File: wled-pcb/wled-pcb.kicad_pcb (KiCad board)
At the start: 2 copper layers, 90.2 x 90.2 mm, 36 parts, among them J2 Conn_02x03_Counter_Clockwise, J3 Screw_Terminal_01x03, J4 Screw_Terminal_01x03, J5 Screw_Terminal_01x03, J6 Screw_Terminal_01x02, J7 Screw_Terminal_01x03, K1 Relay_SPDT, Q1 BC337, SW1 SW_Push, SW2 SW_Push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

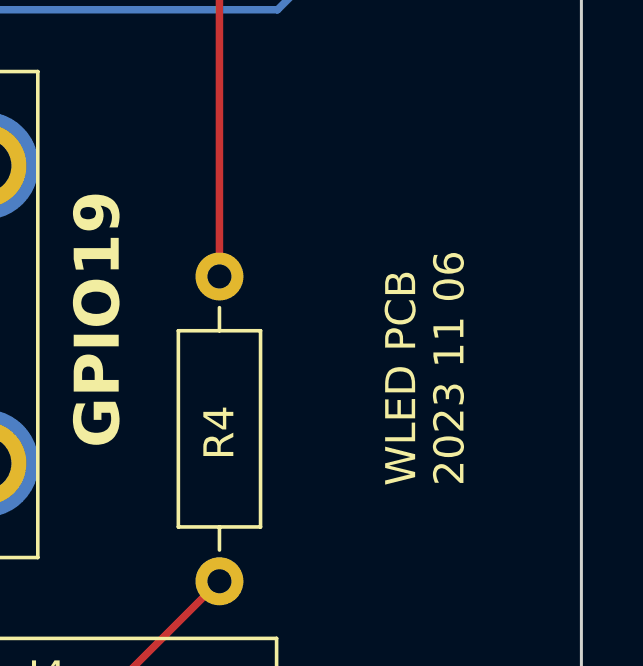
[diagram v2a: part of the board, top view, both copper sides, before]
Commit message: Rotate spokes to pass DRC
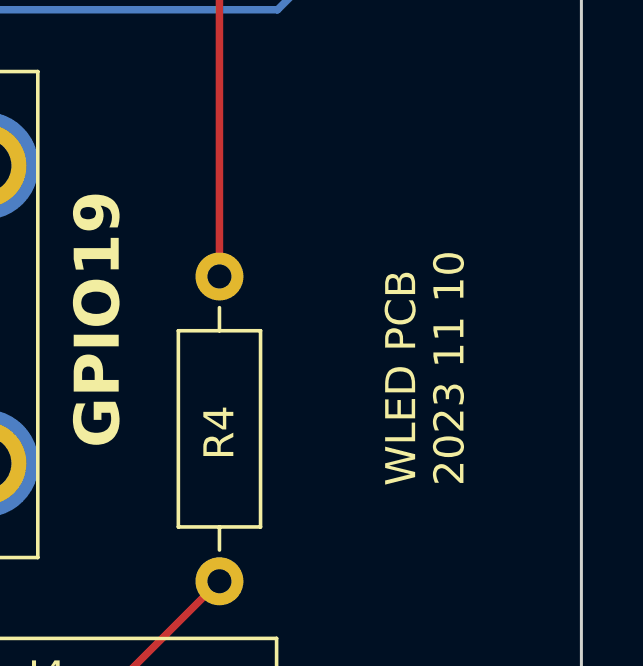
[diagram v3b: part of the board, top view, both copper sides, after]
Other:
- board text added: "WLED PCB 2023 11 10"
- board text removed: "WLED PCB 2023 11 06"
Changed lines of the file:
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@@
       (net 56 "/led3 lo") (pinfunction "D") (pintype "input"))
     (pad "10" thru_hole oval (at 7.62 10.16 90) (size 2.4 1.6) (drill 0.8) (layers "*.Cu" "*.Mask")
-      (net 2 "GND") (pinfunction "EN") (pintype "input"))
+      (net 2 "GND") (pinfunction "EN") (pintype "input") (thermal_bridge_angle 45))
     (pad "11" thru_hole oval (at 7.62 7.62 90) (size 2.4 1.6) (drill 0.8) (layers "*.Cu" "*.Mask")
       (net 26 "Net-(U2D-O)") (pinfunction "O") (pintype "tri_state"))
@@
       (net 39 "/led4 lo") (pinfunction "D") (pintype "input"))
     (pad "13" thru_hole oval (at 7.62 2.54 90) (size 2.4 1.6) (drill 0.8) (layers "*.Cu" "*.Mask")
-      (net 2 "GND") (pinfunction "EN") (pintype "input"))
+      (net 2 "GND") (pinfunction "EN") (pintype "input") (thermal_bridge_angle 45))
     (pad "14" thru_hole oval (at 7.62 0 90) (size 2.4 1.6) (drill 0.8) (layers "*.Cu" "*.Mask")
       (net 1 "+5V") (pinfunction "VCC") (pintype "power_in"))
@@
     (effects (font (size 1.5 1.5) (thickness 0.3) bold) (justify left bottom))
   )
-  (gr_text "WLED PCB\n2023 11 06" (at 180.975 128.27 90) (layer "F.SilkS")
+  (gr_text "WLED PCB\n2023 11 10" (at 180.975 128.27 90) (layer "F.SilkS")
     (effects (font (size 1 1) (thickness 0.15)) (justify left bottom))
   )

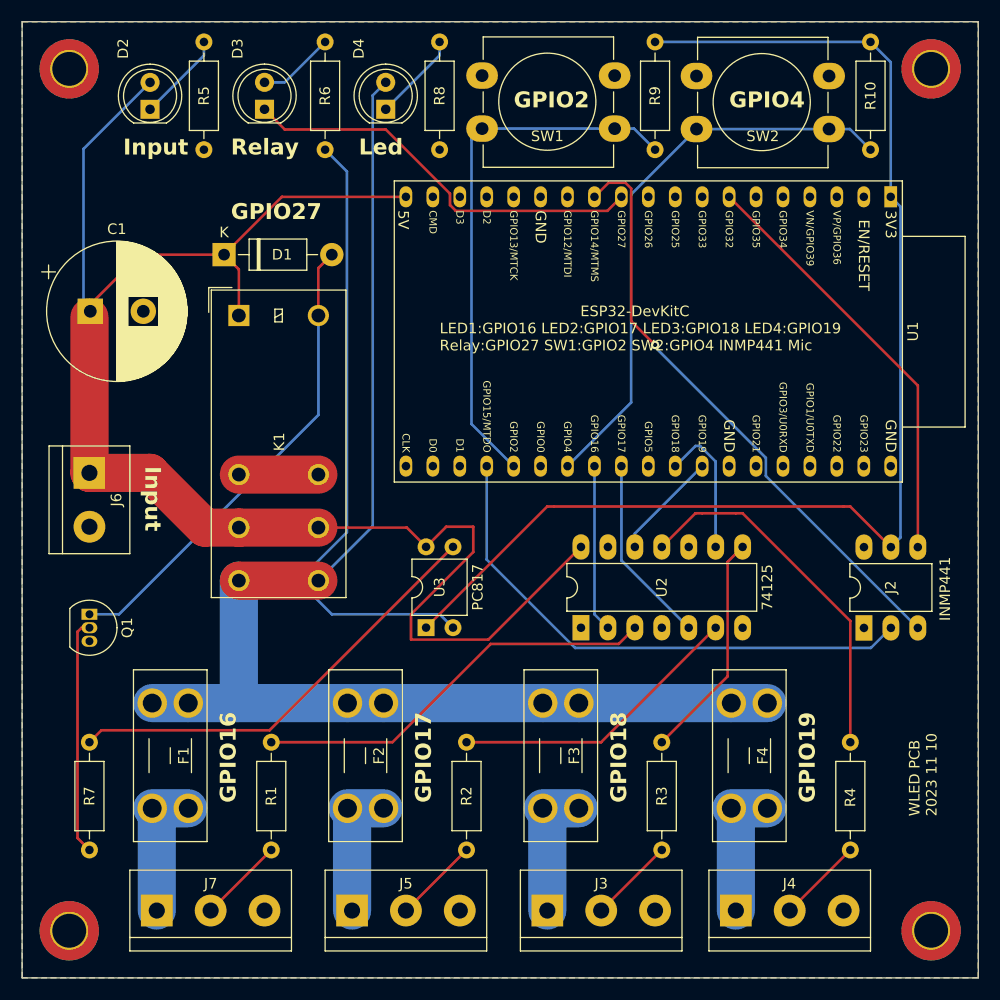
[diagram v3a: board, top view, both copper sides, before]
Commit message: Duplicate power traces on both sides of PCB
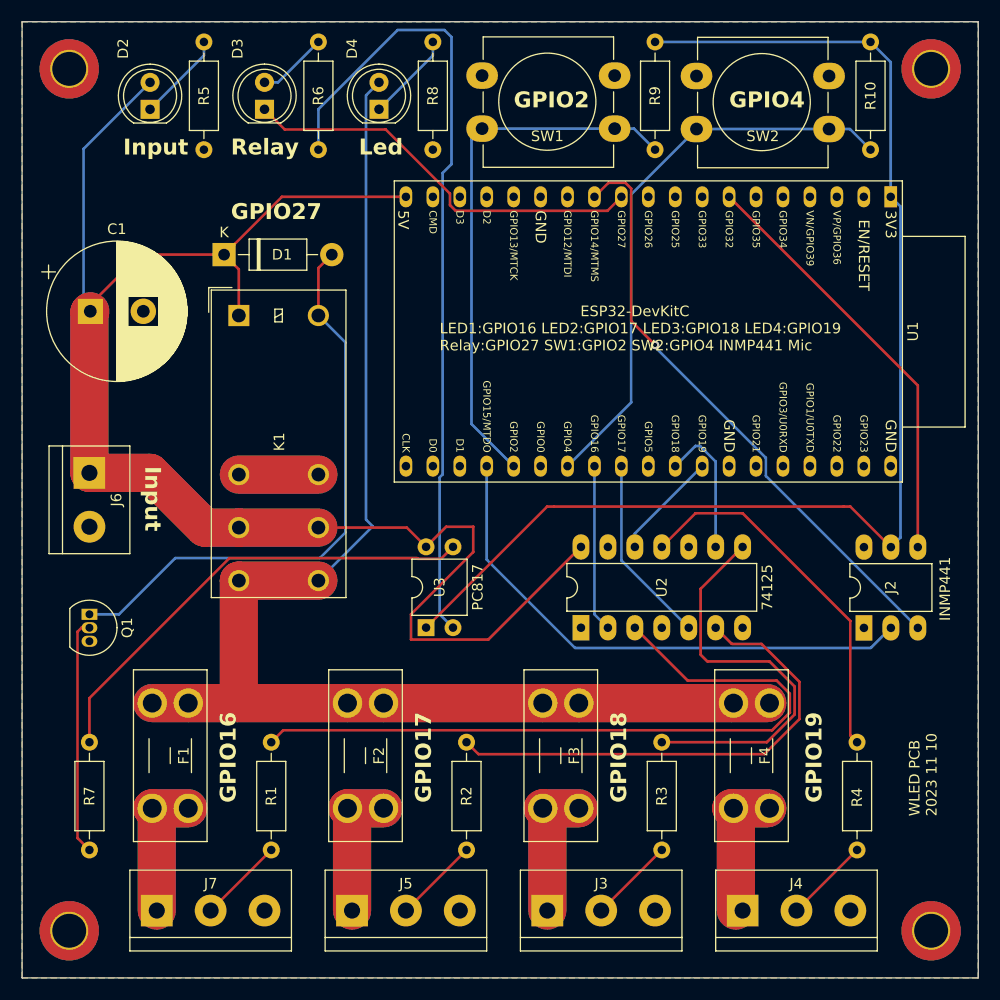
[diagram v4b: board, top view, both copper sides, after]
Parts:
- moved R8 0.64 mm to (133.3, 65.4)
- moved D4 0.63 mm to (128.3, 61.6)
- moved J4 0.63 mm to (162.6, 137.2)
- moved R4 0.63 mm to (173.4, 131.4)
- moved R6 0.63 mm to (122.6, 65.4)
- moved F4 0.20 mm to (165.1, 117.6)
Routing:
- net /5v sw: track 126.7 -> 204.1 mm
- net +5V: track 153.4 -> 193.0 mm
- net Net-(U2A-O): track 38.8 -> 69.0 mm
- net Net-(U2B-O): track 28.0 -> 46.8 mm
- net Net-(R6-Pad1): track 59.4 -> 76.4 mm
- net Net-(U2C-O): track 21.6 -> 38.2 mm
- net Net-(J4-Pin_1): track 13.2 -> 26.4 mm
- net Net-(J3-Pin_1): track 13.2 -> 26.4 mm
- net Net-(J5-Pin_1): track 13.2 -> 26.4 mm
- net Net-(J7-Pin_1): track 13.2 -> 26.4 mm
- net Net-(D1-A): track 45.0 -> 55.1 mm
- net unconnected-(K1-Pad12): track 7.50 -> 15.0 mm
- net Net-(R7-Pad2): track 41.9 -> 44.4 mm
- net Net-(D3-A): track 7.29 -> 6.66 mm

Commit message: Add connector text
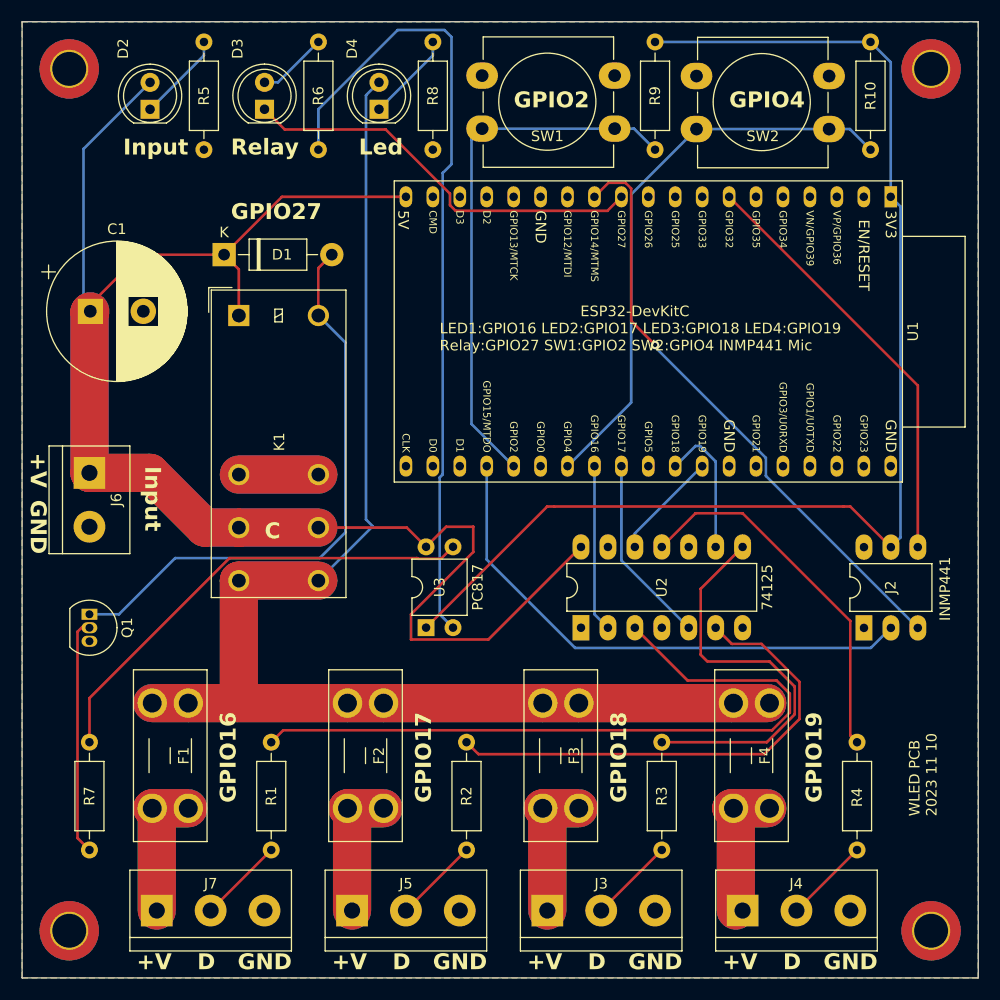
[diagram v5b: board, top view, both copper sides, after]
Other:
- board text added: "+V"
- board text added: "C"
- board text added: "D"
- board text added: "GND"
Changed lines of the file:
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@@
   (gr_rect (start 94.615 53.34) (end 184.785 143.51)
     (stroke (width 0.1) (type default)) (fill none) (layer "Edge.Cuts"))
+  (gr_text "GND" (at 151.765 142.875) (layer "F.SilkS")
+    (effects (font (size 1.5 1.5) (thickness 0.3) bold) (justify left bottom))
+  )
+  (gr_text "GND" (at 114.935 142.875) (layer "F.SilkS")
+    (effects (font (size 1.5 1.5) (thickness 0.3) bold) (justify left bottom))
+  )
   (gr_text "GPIO2" (at 140.97 61.595) (layer "F.SilkS")
+    (effects (font (size 1.5 1.5) (thickness 0.3) bold) (justify left bottom))
+  )
+  (gr_text "D" (at 147.955 142.875) (layer "F.SilkS")
     (effects (font (size 1.5 1.5) (thickness 0.3) bold) (justify left bottom))
   )
@@
     (effects (font (size 1 1) (thickness 0.15)) (justify left bottom))
   )
+  (gr_text "GND" (at 95.25 98.425 -90) (layer "F.SilkS")
+    (effects (font (size 1.5 1.5) (thickness 0.3) bold) (justify left bottom))
+  )
+  (gr_text "D" (at 129.54 142.875) (layer "F.SilkS")
+    (effects (font (size 1.5 1.5) (thickness 0.3) bold) (justify left bottom))
+  )
+  (gr_text "+V" (at 95.25 93.98 -90) (layer "F.SilkS")
+    (effects (font (size 1.5 1.5) (thickness 0.3) bold) (justify left bottom))
+  )
   (gr_text "GPIO4" (at 161.29 61.595) (layer "F.SilkS")
     (effects (font (size 1.5 1.5) (thickness 0.3) bold) (justify left bottom))
@@
     (effects (font (size 1.5 1.5) (thickness 0.3) bold) (justify left bottom))
   )
+  (gr_text "D" (at 166.37 142.875) (layer "F.SilkS")
+    (effects (font (size 1.5 1.5) (thickness 0.3) bold) (justify left bottom))
+  )
   (gr_text "GPIO27" (at 114.3 72.1275) (layer "F.SilkS")
+    (effects (font (size 1.5 1.5) (thickness 0.3) bold) (justify left bottom))
+  )
+  (gr_text "C" (at 117.475 102.235) (layer "F.SilkS")
+    (effects (font (size 1.5 1.5) (thickness 0.3) bold) (justify left bottom))
+  )
+  (gr_text "+V" (at 142.24 142.875) (layer "F.SilkS")
     (effects (font (size 1.5 1.5) (thickness 0.3) bold) (justify left bottom))
   )
@@
   )
   (gr_text "GPIO19" (at 170.18 127 90) (layer "F.SilkS")
+    (effects (font (size 1.5 1.5) (thickness 0.3) bold) (justify left bottom))
+  )
+  (gr_text "+V" (at 105.41 142.875) (layer "F.SilkS")
     (effects (font (size 1.5 1.5) (thickness 0.3) bold) (justify left bottom))
   )
@@
     (effects (font (size 1.5 1.5) (thickness 0.3) bold) (justify left bottom))
   )
+  (gr_text "+V" (at 160.655 142.875) (layer "F.SilkS")
+    (effects (font (size 1.5 1.5) (thickness 0.3) bold) (justify left bottom))
+  )
+  (gr_text "D" (at 111.125 142.875) (layer "F.SilkS")
+    (effects (font (size 1.5 1.5) (thickness 0.3) bold) (justify left bottom))
+  )
   (gr_text "INMP441" (at 182.245 109.855 90) (layer "F.SilkS")
     (effects (font (size 1 1) (thickness 0.15)) (justify left bottom))
   )
+  (gr_text "+V" (at 123.825 142.875) (layer "F.SilkS")
+    (effects (font (size 1.5 1.5) (thickness 0.3) bold) (justify left bottom))
+  )
+  (gr_text "GND" (at 170.18 142.875) (layer "F.SilkS")
+    (effects (font (size 1.5 1.5) (thickness 0.3) bold) (justify left bottom))
+  )
+  (gr_text "GND" (at 133.35 142.875) (layer "F.SilkS")
+    (effects (font (size 1.5 1.5) (thickness 0.3) bold) (justify left bottom))
+  )
   (gr_text "LED1:GPIO16 LED2:GPIO17 LED3:GPIO18 LED4:GPIO19\nRelay:GPIO27 SW1:GPIO2 SW2:GPIO4 INMP441 Mic" (at 133.985 84.455) (layer "F.SilkS")

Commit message: Add more info to silkscreen
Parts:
- R5, R8: value 150R -> 1K
- R6: value R -> 150R
- R7: value R -> 1K
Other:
- board text added: "L/R"
- board text added: "SCK"
- board text added: "SD"
- board text added: "VDD"
- board text added: "WS"
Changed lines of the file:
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@@
         (effects (font (size 1 1) (thickness 0.15)))
     )
-    (fp_text value "1N4001" (at 5.08 2.47) (layer "F.Fab")
+    (fp_text value "1N4001" (at 5.08 2.47) (layer "F.SilkS")
         (effects (font (size 1 1) (thickness 0.15)))
     )
@@
         (effects (font (size 1 1) (thickness 0.15)))
     )
-    (fp_text value "10k" (at 5.08 2.37 90) (layer "F.Fab")
+    (fp_text value "10k" (at 5.08 2.37 90) (layer "F.SilkS")
         (effects (font (size 1 1) (thickness 0.15)))
     )
@@
         (effects (font (size 1 1) (thickness 0.15)))
     )
-    (fp_text value "62R" (at 5.08 2.37 90) (layer "F.Fab")
+    (fp_text value "62R" (at 5.08 2.37 90) (layer "F.SilkS")
         (effects (font (size 1 1) (thickness 0.15)))
     )
@@
         (effects (font (size 1 1) (thickness 0.15)))
     )
-    (fp_text value "R" (at 5.08 2.37 90) (layer "F.Fab")
+    (fp_text value "150R" (at 5.08 2.37 90) (layer "F.SilkS")
         (effects (font (size 1 1) (thickness 0.15)))
     )
@@
         (effects (font (size 1 1) (thickness 0.15)))
     )
-    (fp_text value "10k" (at 5.08 2.37 90) (layer "F.Fab")
+    (fp_text value "10k" (at 5.08 2.37 90) (layer "F.SilkS")
         (effects (font (size 1 1) (thickness 0.15)))
     )
@@
         (effects (font (size 1 1) (thickness 0.15)))
     )
-    (fp_text value "62R" (at 5.08 2.37 90) (layer "F.Fab")
+    (fp_text value "62R" (at 5.08 2.37 90) (layer "F.SilkS")
         (effects (font (size 1 1) (thickness 0.15)))
     )
@@
         (effects (font (size 1 1) (thickness 0.15)))
     )
-    (fp_text value "R" (at 5.08 2.37 90) (layer "F.Fab")
+    (fp_text value "1K" (at 5.08 2.37 90) (layer "F.SilkS")
         (effects (font (size 1 1) (thickness 0.15)))
     )
@@
         (effects (font (size 1 1) (thickness 0.15)))
     )
-    (fp_text value "150R" (at 5.08 2.37 90) (layer "F.Fab")
+    (fp_text value "1K" (at 5.08 2.37 90) (layer "F.SilkS")
         (effects (font (size 1 1) (thickness 0.15)))
     )
@@
         (effects (font (size 1 1) (thickness 0.15)))
     )
-    (fp_text value "BC337" (at 1.27 2.79 90) (layer "F.Fab")
+    (fp_text value "BC337" (at 1.27 2.79 90) (layer "F.SilkS")
         (effects (font (size 1 1) (thickness 0.15)))
     )
@@
         (effects (font (size 1 1) (thickness 0.15)))
     )
-    (fp_text value "1000uF" (at 2.5 7.75) (layer "F.Fab")
+    (fp_text value "1000uF" (at 2.46 8.255) (layer "F.SilkS")
         (effects (font (size 1 1) (thickness 0.15)))
     )
@@
         (effects (font (size 1 1) (thickness 0.15)))
     )
-    (fp_text value "62R" (at 5.08 2.37 90) (layer "F.Fab")
+    (fp_text value "62R" (at 5.08 2.37 90) (layer "F.SilkS")
         (effects (font (size 1 1) (thickness 0.15)))
     )
@@
         (effects (font (size 1 1) (thickness 0.15)))
     )
-    (fp_text value "150R" (at 5.08 2.37 90) (layer "F.Fab")
+    (fp_text value "1K" (at 5.08 2.37 90) (layer "F.SilkS")
         (effects (font (size 1 1) (thickness 0.15)))
     )
@@
         (effects (font (size 1 1) (thickness 0.15)))
     )
-    (fp_text value "62R" (at 5.08 2.37 90) (layer "F.Fab")
+    (fp_text value "62R" (at 5.08 2.37 90) (layer "F.SilkS")
         (effects (font (size 1 1) (thickness 0.15)))
     )
@@
     (effects (font (size 1.5 1.5) (thickness 0.3) bold) (justify left bottom))
   )
+  (gr_text "GND" (at 174.625 101.6 90) (layer "F.SilkS")
+    (effects (font (size 1 1) (thickness 0.15)) (justify left bottom))
+  )
+  (gr_text "L/R" (at 174.625 114.935 90) (layer "F.SilkS")
+    (effects (font (size 1 1) (thickness 0.15)) (justify left bottom))
+  )
   (gr_text "GPIO2" (at 140.97 61.595) (layer "F.SilkS")
     (effects (font (size 1.5 1.5) (thickness 0.3) bold) (justify left bottom))
@@
     (effects (font (size 1.5 1.5) (thickness 0.3) bold) (justify left bottom))
   )
+  (gr_text "SCK" (at 179.705 114.935 90) (layer "F.SilkS")
+    (effects (font (size 1 1) (thickness 0.15)) (justify left bottom))
+  )
+  (gr_text "VDD" (at 177.165 101.6 90) (layer "F.SilkS")
+    (effects (font (size 1 1) (thickness 0.15)) (justify left bottom))
+  )
   (gr_text "GPIO19" (at 170.18 127 90) (layer "F.SilkS")
     (effects (font (size 1.5 1.5) (thickness 0.3) bold) (justify left bottom))
   )
+  (gr_text "WS" (at 177.165 114.935 90) (layer "F.SilkS")
+    (effects (font (size 1 1) (thickness 0.15)) (justify left bottom))
+  )
   (gr_text "+V" (at 105.41 142.875) (layer "F.SilkS")
     (effects (font (size 1.5 1.5) (thickness 0.3) bold) (justify left bottom))
@@
     (effects (font (size 1 1) (thickness 0.15)) (justify left bottom))
   )
+  (gr_text "SD" (at 179.705 101.6 90) (layer "F.SilkS")
+    (effects (font (size 1 1) (thickness 0.15)) (justify left bottom))
+  )
